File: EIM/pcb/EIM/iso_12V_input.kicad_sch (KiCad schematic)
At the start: 7 parts, among them IC4 ILD213T

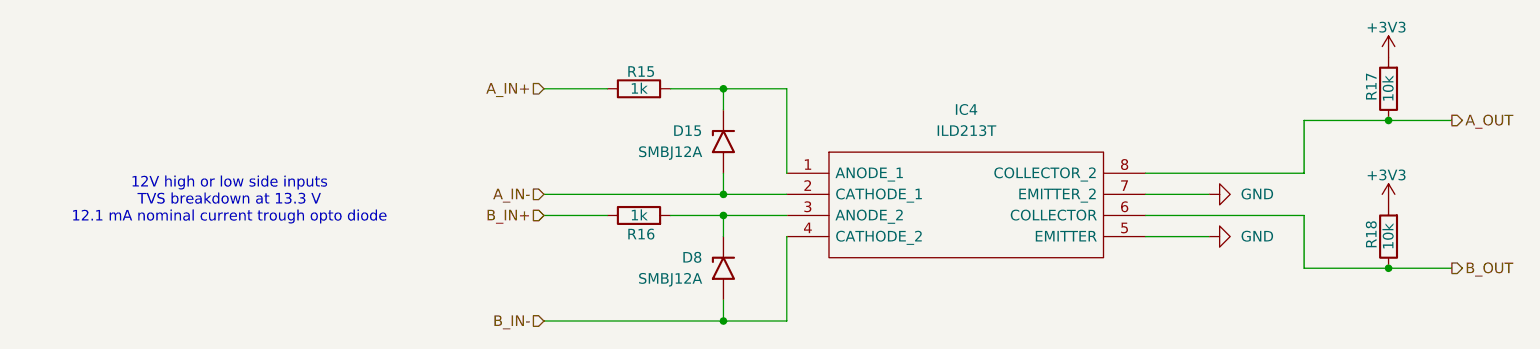
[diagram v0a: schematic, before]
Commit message: added Arjun's comments, assigned some MCU pins
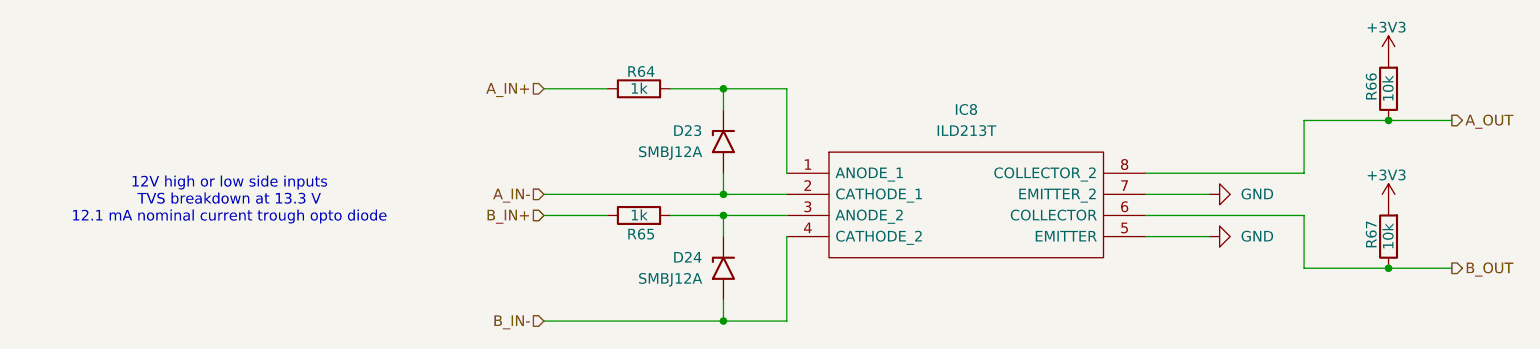
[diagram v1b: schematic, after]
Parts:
- renumbered D15 to D23, D8 to D24, IC4 to IC8, R15 to R64, R16 to R65, R17 to R66, R18 to R67

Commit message: Layout 75% done, before 8V bus deletion
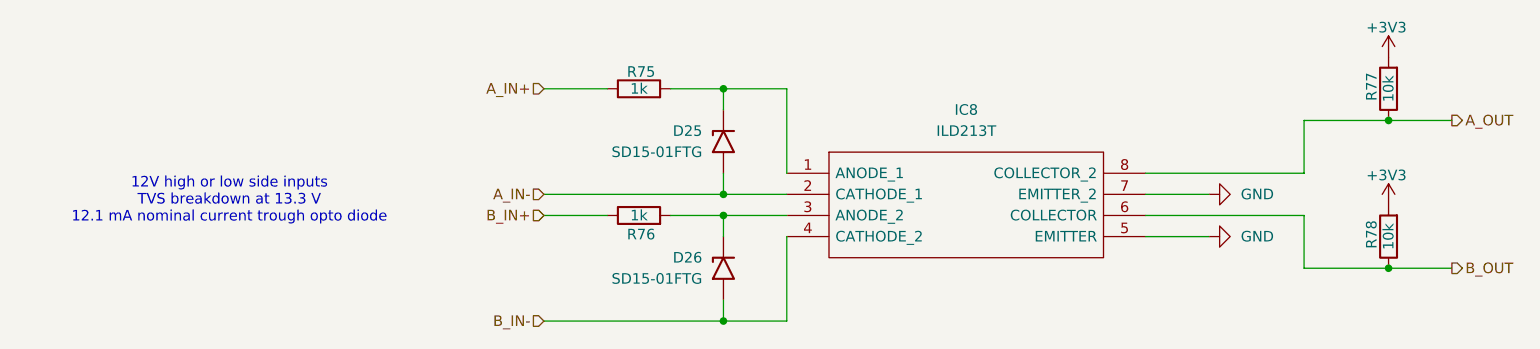
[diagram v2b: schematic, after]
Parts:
- D25: renamed from D23; value SMBJ12A -> SD15-01FTG; footprint Diode_SMD:D_SMB -> Diode_SMD:D_SOD-323
- D26: renamed from D24; value SMBJ12A -> SD15-01FTG; footprint Diode_SMD:D_SMB -> Diode_SMD:D_SOD-323
- renumbered R64 to R75, R65 to R76, R66 to R77, R67 to R78

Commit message: All components placed and pins assigned.
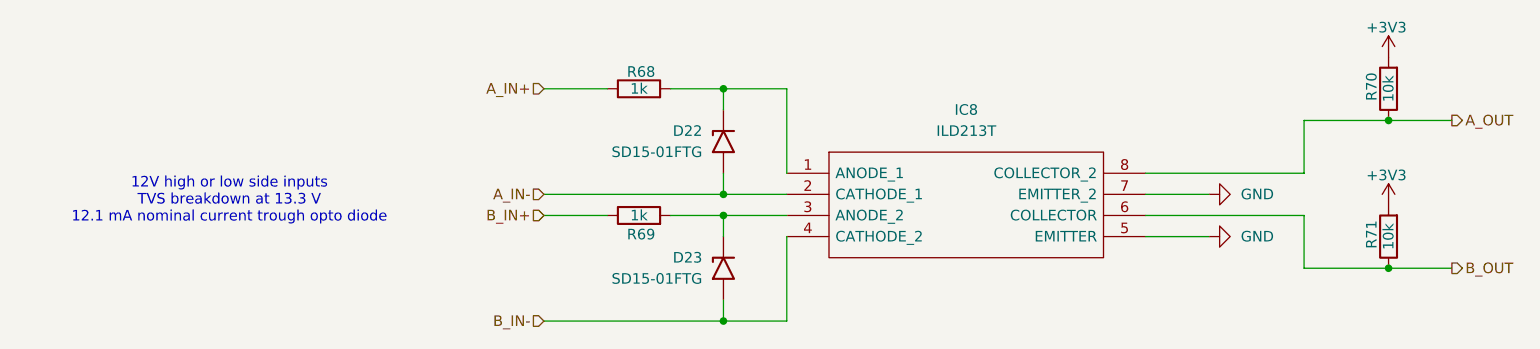
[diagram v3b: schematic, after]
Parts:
- renumbered D25 to D22, D26 to D23, R75 to R68, R76 to R69, R77 to R70, R78 to R71
